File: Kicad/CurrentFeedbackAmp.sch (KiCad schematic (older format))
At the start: 123 parts, among them J1 Test_Etapa_3_Inf, J10 Protecc_Sup_In1, J11 Protecc_Inf_In1, J12 Protecc_Sup_In2, J13 Test_Etapa_3_Inf, J14 Entrada, J15 Salida masa2, J16 Salida tierra, J17 Salida senal, J2 Test_Realim_Out, J3 Salida masa1, J4 Protecc_Sup_Out, J5 Protecc_Inf_Out, J6 Conector Vcc, J7 Conector Vdd, J8 Test_Etapa_3_Inf, J9 Test_Etapa_3_Sup, Q1 TIP42C, Q10 BC858, Q11 BC848, Q12 BC858, Q13 BC559, Q14 BC559, Q15 BC559, Q16 BC549, Q17 BC549, Q18 BC549, Q19 BC559, Q2 BD135, Q20 BC549, Q21 BC559, Q22 BC549, Q23 BC848, Q24 BD136, Q25 BC858, Q26 BC848, Q27 BC848, Q28 BC848, Q29 BC858, Q3 BD136, Q30 BC858, Q31 BC848, Q32 BC858, Q33 BD135, Q34 TIP41C, Q35 BC858, Q36 BC848, Q37 BC848, Q38 BC848, Q4 BC848, Q40 BC858, Q41 BC858, Q5 BC848, Q6 BC858, Q7 BC858, Q8 BC848, Q9 BC858, U1 LM7812_TO220, U2 TL082, U3 LM7912_TO220, U4 LM7805_TO220, U5 LM7905_TO220

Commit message: Cambiadas resistencias SMD por un modelo SMD que es mas grande asi es mas facil de soldar. Tambier cambiamos las resistencias del cuasidarlington de 100 ohm para que sean THT
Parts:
- Q10, Q11, Q12, Q23, Q25, Q26, Q27, Q28, Q29, Q30, Q31, Q32, Q4, Q5, Q6, Q7, Q8, Q9: footprint TO_SOT_Packages_THT:TO-92_Inline_Narrow_Oval -> TO_SOT_Packages_SMD:SOT-23
- R1, R10, R11, R13, R15, R16, R17, R18, R19, R2, R22, R23, R24, R26, R27, R28, R29, R3, R4, R5, R6, R8, R9: footprint Resistors_SMD:R_0805_HandSoldering -> Resistors_SMD:R_1206_HandSoldering
- R20, R21: footprint Resistors_SMD:R_0805_HandSoldering -> Resistors_THT:R_Axial_DIN0414_L11.9mm_D4.5mm_P15.24mm_Horizontal

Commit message: Agregue los modelos para las nuevas resistencias del (ahora unico) multiplicador de Vbe
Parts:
- R12, R30, R31, R32, R7: footprint (none) -> Resistors_SMD:R_1206_HandSoldering
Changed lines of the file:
@@
 F 0 "R12" V 15330 3050 50  0000 C CNN
 F 1 "1k" V 15250 3050 50  0000 C CNN
-F 2 "" V 15180 3050 50  0001 C CNN
+F 2 "Resistors_SMD:R_1206_HandSoldering" V 15180 3050 50  0001 C CNN
 F 3 "" H 15250 3050 50  0001 C CNN
 	1    15250 3050
@@
 F 0 "R7" V 15330 4200 50  0000 C CNN
 F 1 "1k" V 15250 4200 50  0000 C CNN
-F 2 "" V 15180 4200 50  0001 C CNN
+F 2 "Resistors_SMD:R_1206_HandSoldering" V 15180 4200 50  0001 C CNN
 F 3 "" H 15250 4200 50  0001 C CNN
 	1    15250 4200
@@
 F 0 "R31" V 15680 4400 50  0000 C CNN
 F 1 "5.1" V 15600 4400 50  0000 C CNN
-F 2 "" V 15530 4400 50  0001 C CNN
+F 2 "Resistors_SMD:R_1206_HandSoldering" V 15530 4400 50  0001 C CNN
 F 3 "" H 15600 4400 50  0001 C CNN
 	1    15600 4400
@@
 F 0 "R30" V 15680 2900 50  0000 C CNN
 F 1 "5.1" V 15600 2900 50  0000 C CNN
-F 2 "" V 15530 2900 50  0001 C CNN
+F 2 "Resistors_SMD:R_1206_HandSoldering" V 15530 2900 50  0001 C CNN
 F 3 "" H 15600 2900 50  0001 C CNN
 	1    15600 2900
@@
 F 0 "R32" V 15130 3550 50  0000 C CNN
 F 1 "1k" V 15050 3550 50  0000 C CNN
-F 2 "" V 14980 3550 50  0001 C CNN
+F 2 "Resistors_SMD:R_1206_HandSoldering" V 14980 3550 50  0001 C CNN
 F 3 "" H 15050 3550 50  0001 C CNN
 	1    15050 3550

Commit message: Arreglo error en conectores banana de tensiones de alimentacion que tenian el modelo erroneo
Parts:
- J6, J7: footprint Connectors_Terminal_Blocks:TerminalBlock_Pheonix_MKDS1.5-2pol -> Connectors:Banana_Jack_1Pin
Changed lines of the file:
@@
 F 0 "J6" H 20100 1350 50  0000 C CNN
 F 1 "Conector Vcc" H 20100 1150 50  0000 C CNN
-F 2 "Connectors_Terminal_Blocks:TerminalBlock_Pheonix_MKDS1.5-2pol" H 20100 1250 50  0001 C CNN
+F 2 "Connectors:Banana_Jack_1Pin" H 20100 1250 50  0001 C CNN
 F 3 "" H 20100 1250 50  0001 C CNN
 	1    20100 1250
@@
 F 0 "J7" H 20250 5850 50  0000 C CNN
 F 1 "Conector Vdd" H 20250 5650 50  0000 C CNN
-F 2 "Connectors_Terminal_Blocks:TerminalBlock_Pheonix_MKDS1.5-2pol" H 20250 5750 50  0001 C CNN
+F 2 "Connectors:Banana_Jack_1Pin" H 20250 5750 50  0001 C CNN
 F 3 "" H 20250 5750 50  0001 C CNN
 	1    20250 5750

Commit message: reparacion version vieja vs nueva de Kicad. Si van a hacer algo gratuito y libre por lo menos haganlo bien!
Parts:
- C1, C10, C11, C12, C2, C3, C4, C5, C6, C7, C8, C9, CCOMP3, CCOMP4: symbol C -> device:C
- C13, C14: symbol CP -> device:CP
- J1, J10, J11, J12, J13, J15, J16, J17, J2, J3, J4, J5, J6, J7, J8, J9: symbol Conn_01x01 -> CurrentFeedbackAmp-rescue:Conn_01x01
- J14: symbol Conn_Coaxial -> CurrentFeedbackAmp-rescue:Conn_Coaxial
- MK1, MK2, MK3, MK4: symbol Mounting_Hole -> CurrentFeedbackAmp-rescue:Mounting_Hole
- Q1: footprint TO_SOT_Packages_THT:TO-220_Vertical -> TerminalBlock:TerminalBlock_bornier-3_P5.08mm; symbol TIP42C -> CurrentFeedbackAmp-rescue:TIP42C
- Q10, Q12, Q13, Q14, Q15, Q19, Q21, Q25, Q29, Q30, Q32, Q35, Q40, Q41, Q6, Q7, Q9: symbol BC559 -> CurrentFeedbackAmp-rescue:BC559
- Q11, Q16, Q17, Q18, Q20, Q22, Q23, Q26, Q27, Q28, Q31, Q36, Q37, Q38, Q4, Q5, Q8: symbol BC549 -> CurrentFeedbackAmp-rescue:BC549
- Q2, Q33: symbol BD135 -> CurrentFeedbackAmp-rescue:BD135
- Q24, Q3: symbol BD136 -> CurrentFeedbackAmp-rescue:BD136
- Q34: footprint TO_SOT_Packages_THT:TO-220_Vertical -> TerminalBlock:TerminalBlock_bornier-3_P5.08mm; symbol TIP41C -> CurrentFeedbackAmp-rescue:TIP41C
- R12, R30, R31, R7: symbol R -> device:R
- R32: footprint Resistors_SMD:R_1206_HandSoldering -> Resistor_THT:R_Axial_DIN0204_L3.6mm_D1.6mm_P7.62mm_Horizontal; symbol R -> device:R
- Rfino1, Rgrueso1, Rref3: symbol POT-RESCUE-CurrentFeedbackAmp -> CurrentFeedbackAmp-rescue:POT-RESCUE-CurrentFeedbackAmp
- U1: symbol LM7812_TO220 -> CurrentFeedbackAmp-rescue:LM7812_TO220
- U2: symbol TL082 -> CurrentFeedbackAmp-rescue:TL082
- U3: symbol LM7912_TO220 -> CurrentFeedbackAmp-rescue:LM7912_TO220
- U4: symbol LM7805_TO220 -> CurrentFeedbackAmp-rescue:LM7805_TO220
- U5: symbol LM7905_TO220 -> CurrentFeedbackAmp-rescue:LM7905_TO220
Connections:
- wire segments 223 -> 312

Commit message: Esquematico de Kicad actualizado
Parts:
- added CN1, CN2: 100n, Capacitors_THT:C_Disc_D5.0mm_W2.5mm_P5.00mm, symbol device:C
- added RE1, RE2: 10, Resistors_SMD:R_1206_HandSoldering, symbol pspice:R
- added RN1, RN2: 18k, Resistors_SMD:R_1206_HandSoldering, symbol pspice:R
- Q20, Q22: value BC549 -> BD135
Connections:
- wire segments 312 -> 241
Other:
- moved on the sheet: C1, C2, Q13, Q14, Q31, Q32

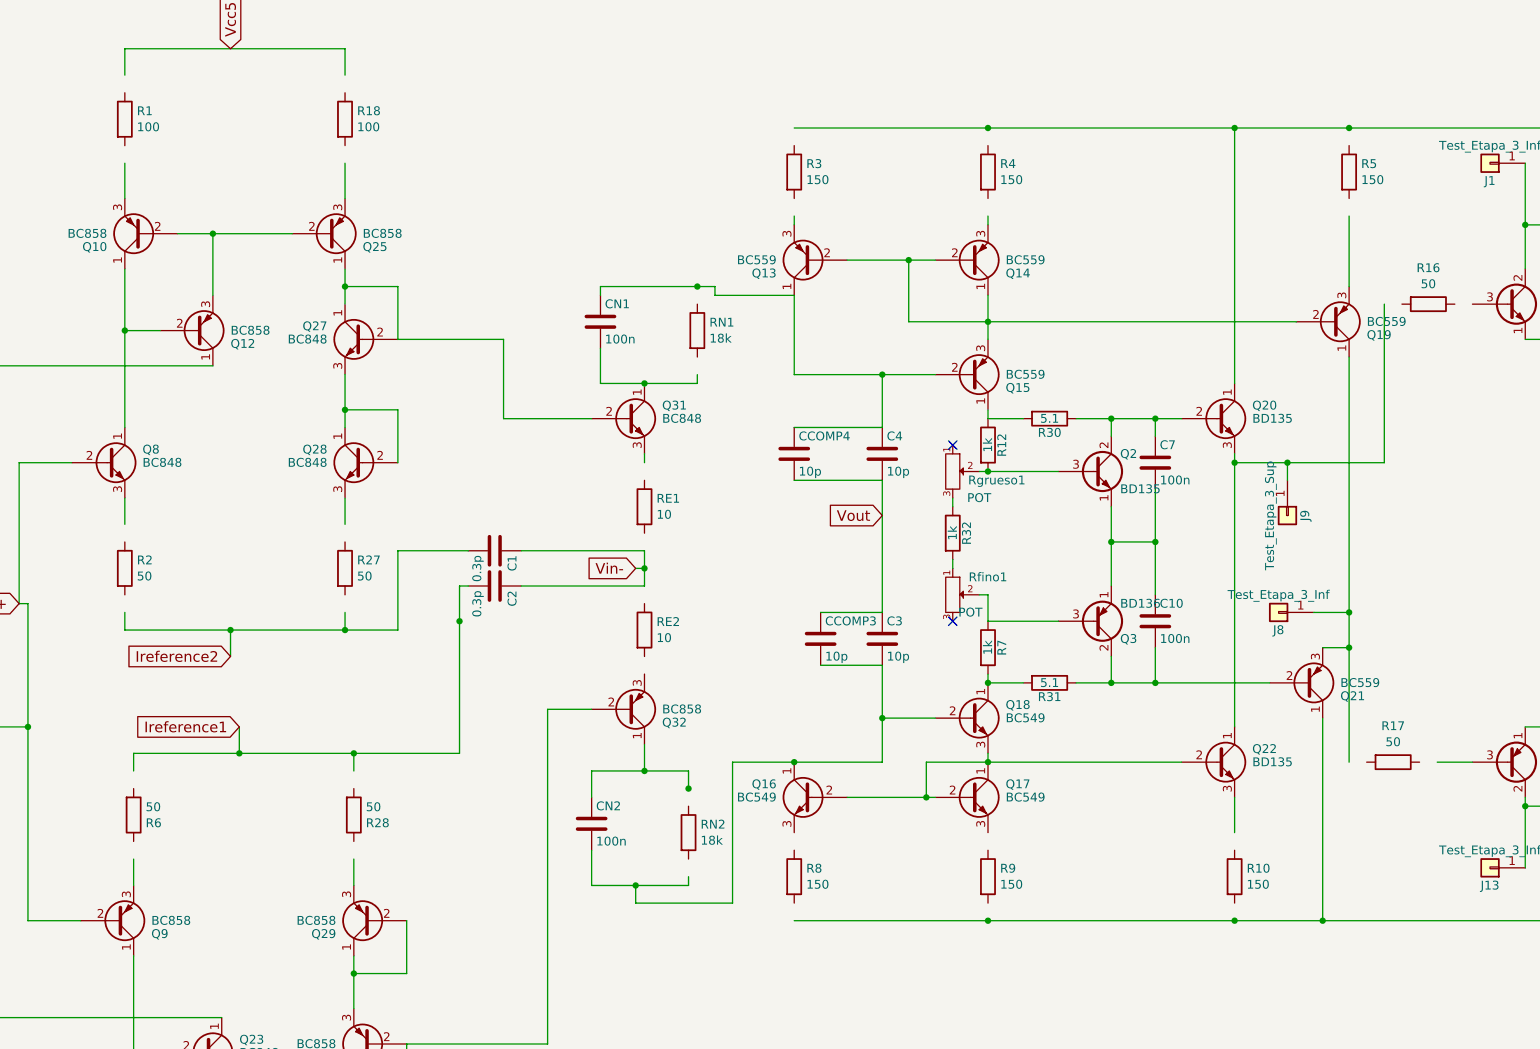
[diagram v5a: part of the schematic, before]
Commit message: va el circuito sin muchas cosas que sobraban
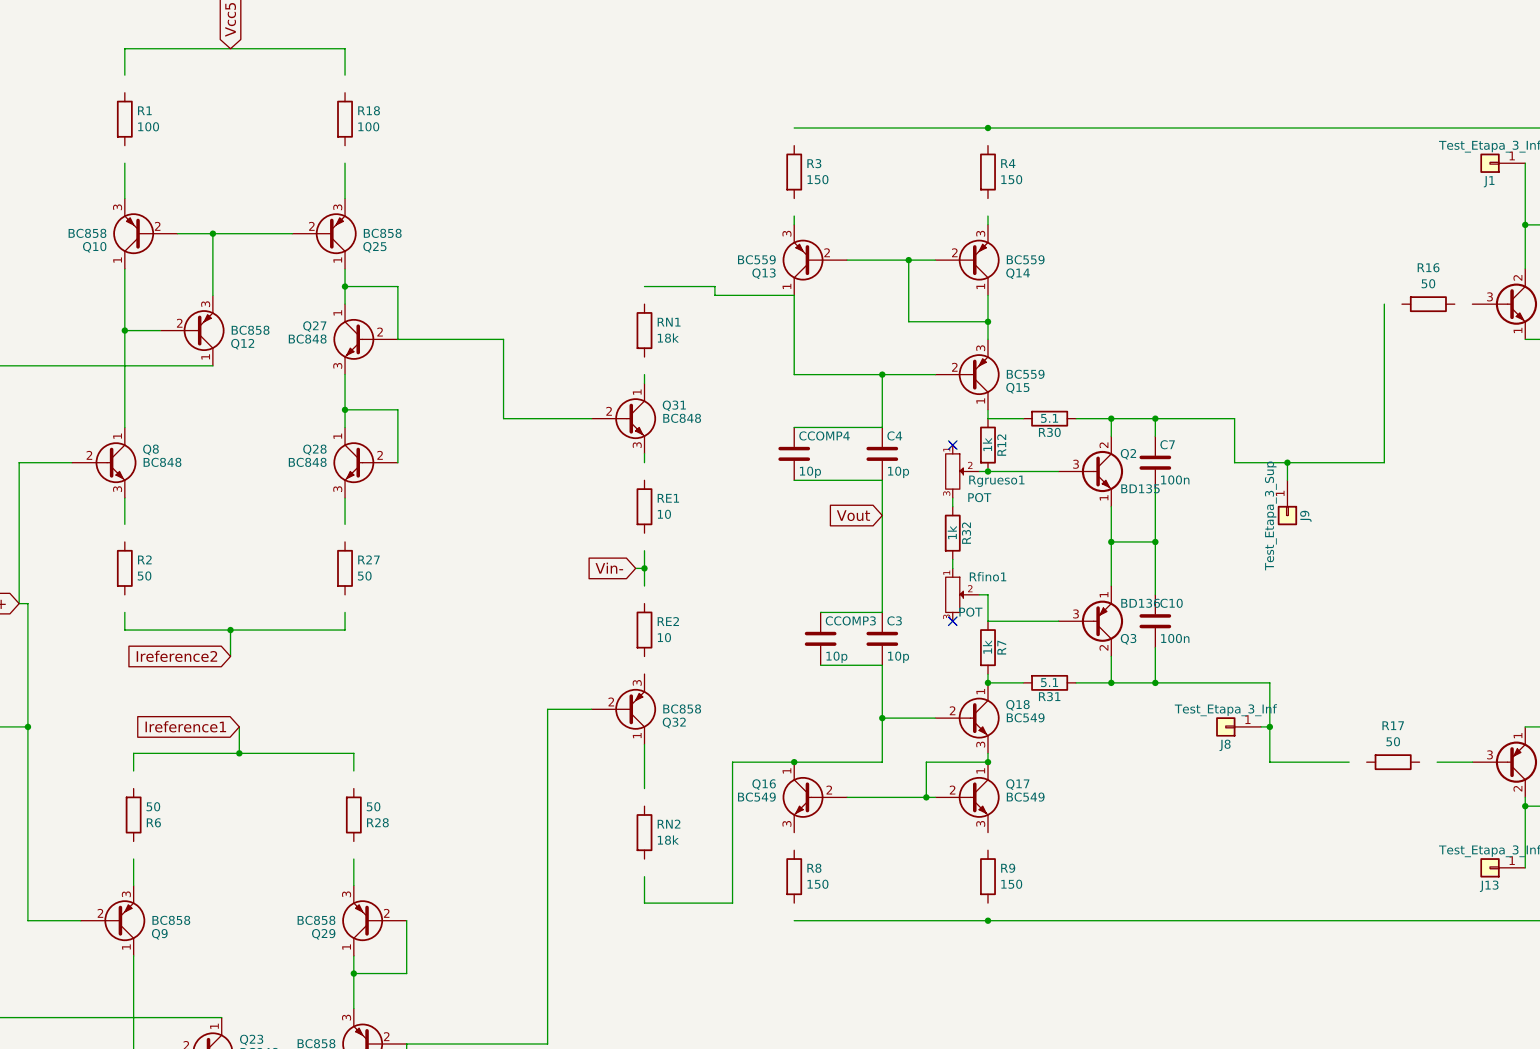
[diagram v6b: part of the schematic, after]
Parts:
- removed C1, C2: 0.3p, Capacitors_THT:C_Disc_D5.0mm_W2.5mm_P5.00mm, symbol device:C
- removed CN1, CN2: 100n, Capacitors_THT:C_Disc_D5.0mm_W2.5mm_P5.00mm, symbol device:C
- removed Q19, Q21: BC559, TO_SOT_Packages_THT:TO-92_Inline_Narrow_Oval, symbol CurrentFeedbackAmp-rescue:BC559
- removed Q20, Q22: BD135, TO_SOT_Packages_THT:TO-92_Inline_Narrow_Oval, symbol CurrentFeedbackAmp-rescue:BC549
- removed R10, R5: 150, Resistors_SMD:R_1206_HandSoldering, symbol pspice:R
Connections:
- wire segments 241 -> 222
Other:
- moved on the sheet: J8, RN1, RN2
